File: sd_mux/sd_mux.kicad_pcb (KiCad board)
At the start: 2 copper layers, 86.4 x 54.6 mm, 22 parts, among them IC1 SN74CBT3257DR, IC2 SN74CBT3257DR, J1 Micro_SD_Card_Det, J2 DEVICE 1, J3 DEVICE 2, J4 CONTROL

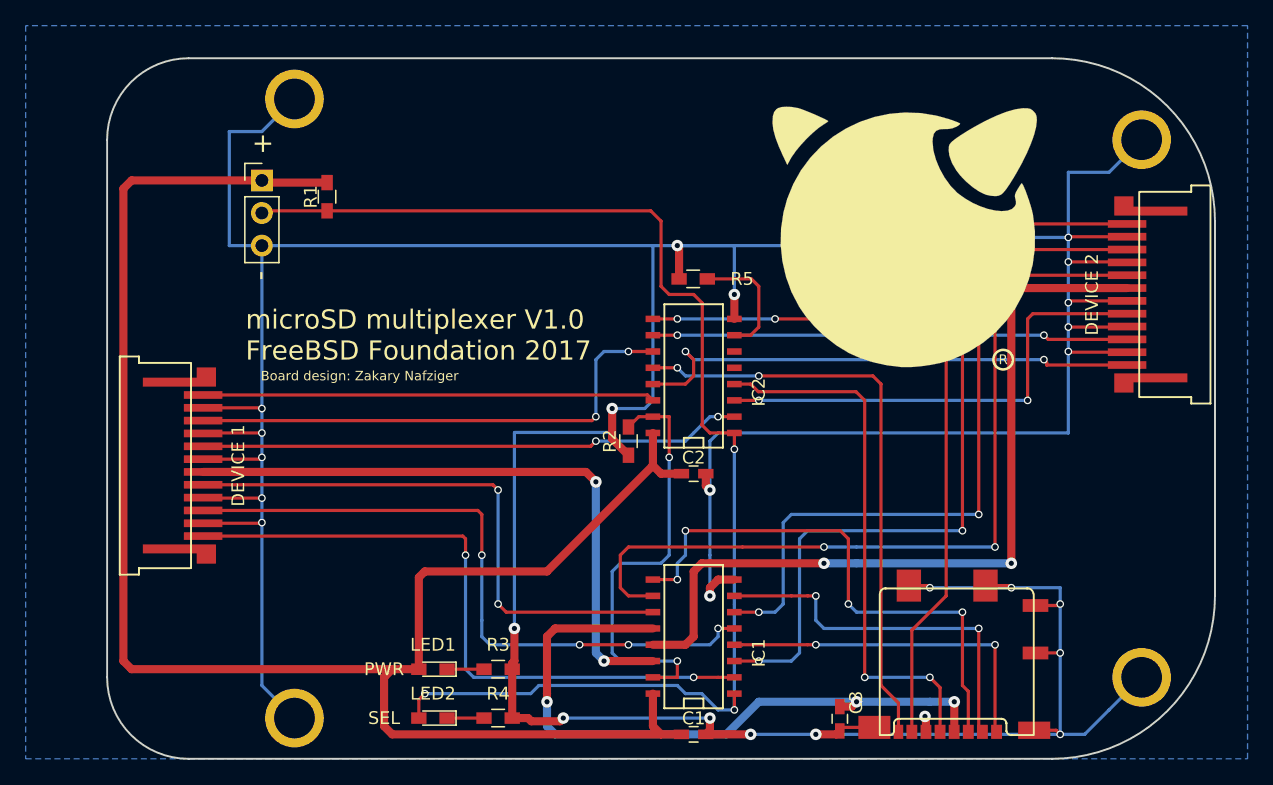
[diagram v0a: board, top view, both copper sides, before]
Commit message: Use the SN74CB3Q3257.
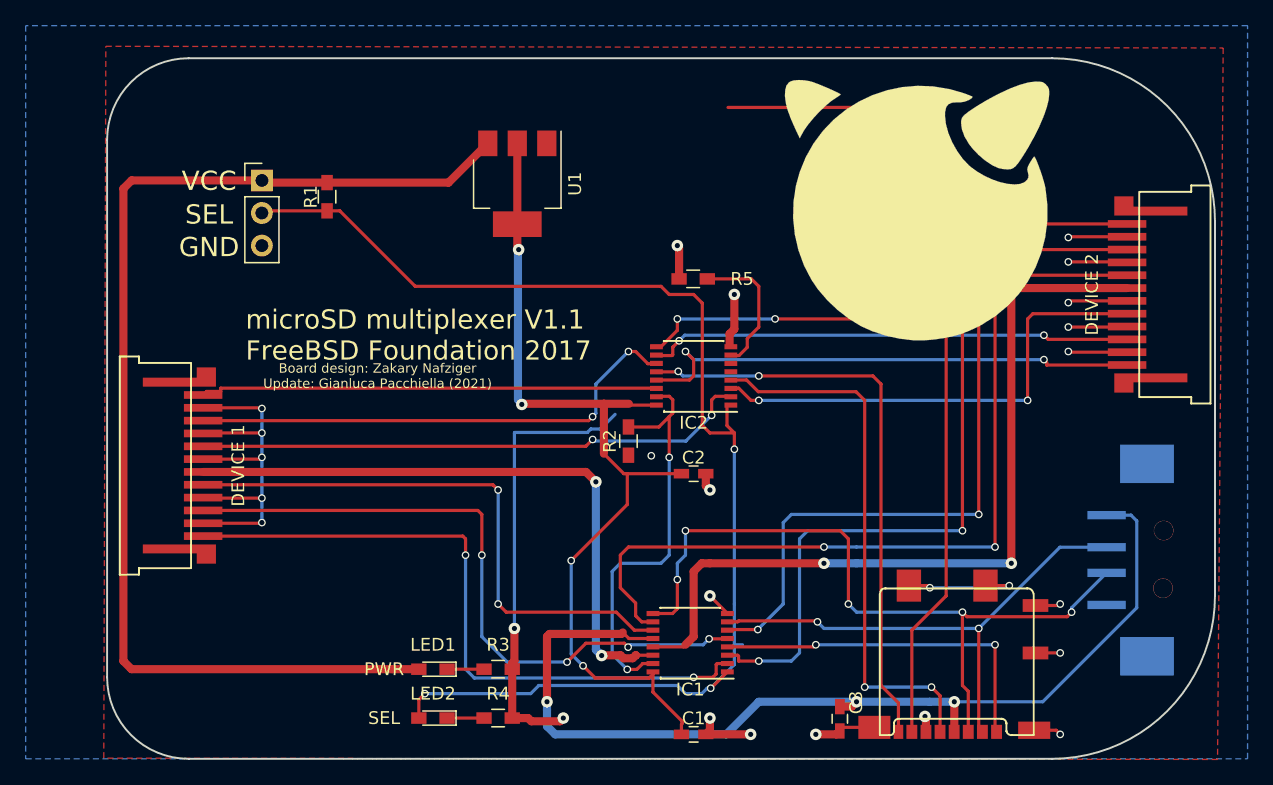
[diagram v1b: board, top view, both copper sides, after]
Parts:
- removed the G*** at (146.1, 94.6)
- removed the G*** at (163.8, 81.3)
- removed REF** (x4): 125mil_plated_mounting_hole, sd_mux_footprints:125mil_plated_mounting_hole
- added G***: LOGO, sd_mux_footprints:fbsd_logo, F.Cu at (164.8, 79.2)
- added G***: LOGO, Symbol:avatar, B.Cu at (159.2, 78.6)
- added J5: USB_A, Connector_USB:USB aliexpress, B.Cu at (183.9, 106.4)
- added U1: AMS1117-3.3, Package_TO_SOT_SMD:SOT-223-3_TabPin2, F.Cu at (133.6, 77.1)
- IC1, IC2: value SN74CBT3257DR -> SN74CB3Q3257DBQR; footprint SMD_Packages:SO-16-N -> Package_SO:SSOP-16_4.4x5.2mm_P0.65mm
- moved IC1 0.55 mm to (147.1, 112.9), turned to 180 degrees
- turned IC2 to 180 degrees
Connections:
- net DAT3/CD_1 renamed DAT3/CD_1
- net DAT3/CD_2 renamed DAT3/CD_2
- net Net-(C3-Pad1) renamed VDD
- net Net-(IC1-Pad7) renamed DAT3/CD
- net Net-(IC1-Pad9) renamed CMD
- C1 pad 1: VCC -> 3V3
- C2 pad 1: VCC -> 3V3
- IC1 pad 16: VCC -> 3V3
- IC2 pad 16: VCC -> 3V3
- IC2 pad 5: Net-(IC2-Pad5) -> (no net)
- IC2 pad 6: Net-(IC2-Pad6) -> (no net)
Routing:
- net GND: track 392.1 -> 128.5 mm
- net 3V3: track 0.00 -> 70.7 mm, vias 0 -> 4
- net VCC: track 142.0 -> 90.1 mm
- net VDD: track 52.4 -> 79.0 mm
- net CMD: track 42.7 -> 58.1 mm, vias 4 -> 5
- net DAT3/CD: track 29.4 -> 40.6 mm
- net (no net): track 0.00 -> 10.0 mm
- net device_select: track 103.4 -> 100.4 mm
- net OE: track 34.1 -> 32.1 mm
- net Net-(IC2-Pad7): track 9.60 -> 11.2 mm
- net CMD_2: track 66.2 -> 67.6 mm
- net DAT3/CD_2: track 57.9 -> 59.1 mm
- net CLK_2: track 37.1 -> 38.1 mm
- net DAT2_2: track 63.7 -> 64.7 mm
- net CLK_1: track 42.4 -> 43.3 mm
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- added copper zone on F.Cu, net GND
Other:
- net class Default removed
- board text added: "Board design: Zakary Nafziger Update: Gianluca Pacchiella (2021)"
- board text added: "Electrical characteristics"
- board text added: "GND"
- board text added: "Input voltage (VCC) 15V - 4.6V Select voltage (SEL) 3.3V - 2.5V"
- board text added: "SEL"
- board text added: "TODO: put a led for each output near it"
- board text added: "VCC"
- board text added: "microSD multiplexer V1.1 FreeBSD Foundation 2017"
- board text removed: "+"
- board text removed: "-"
- board text removed: "Board design: Zakary Nafziger"
- board text removed: "R"
- board text removed: "microSD multiplexer V1.0 FreeBSD Foundation 2017"
